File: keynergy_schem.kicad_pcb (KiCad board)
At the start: 2 copper layers, 0 parts

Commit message: new updates
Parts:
- added REF**: Solenoid Key, project library:Untitled, F.Cu at (56.3, 88.2)

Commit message: new update
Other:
- board outline added: 196 x 79.8 mm
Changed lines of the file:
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@@
 		(at 56.272 88.225312)
 		(property "Reference" "REF**"
-			(at 0 -0.5 0)
+			(at 0 8.128 0)
 			(unlocked yes)
 			(layer "F.SilkS")
@@
 		)
 		(property "Value" "Solenoid Key"
-			(at 0 1 0)
+			(at -0.127 9.652 0)
 			(unlocked yes)
 			(layer "F.Fab")
@@
 			(layer "F.SilkS")
 		)
+		(fp_rect
+			(start -4.4915 -4.4915)
+			(end 4.5085 4.5085)
+			(stroke
+				(width 0.05)
+				(type solid)
+			)
+			(fill yes)
+			(layer "Edge.Cuts")
+		)
 		(fp_text user "${REFERENCE}"
-			(at 0 2.5 0)
+			(at -0.254 11.43 0)
 			(unlocked yes)
 			(layer "F.Fab")
@@
 		)
 		(pad "1" smd roundrect
-			(at -14.4145 -0.0635)
-			(size 2.159 7.493)
+			(at -14.4145 0)
+			(size 2.159 7.366)
 			(layers "F.Cu" "F.Mask" "F.Paste")
 			(roundrect_rratio 0)
@@
 	)
 	(gr_rect
-		(start 26.1 23.6)
-		(end 222.1 98.3)
-		(stroke
-			(width 0.2)
-			(type default)
-		)
-		(fill no)
-		(layer "F.Cu")
-	)
-	(gr_rect
 		(start 123.6 56)
 		(end 125.1 61.8)
@@
 	)
 	(gr_rect
+		(start 26.1 23.6)
+		(end 222.1 103.38)
+		(stroke
+			(width 0.2)
+			(type solid)
+		)
+		(fill no)
+		(layer "Edge.Cuts")
+	)
+	(gr_rect

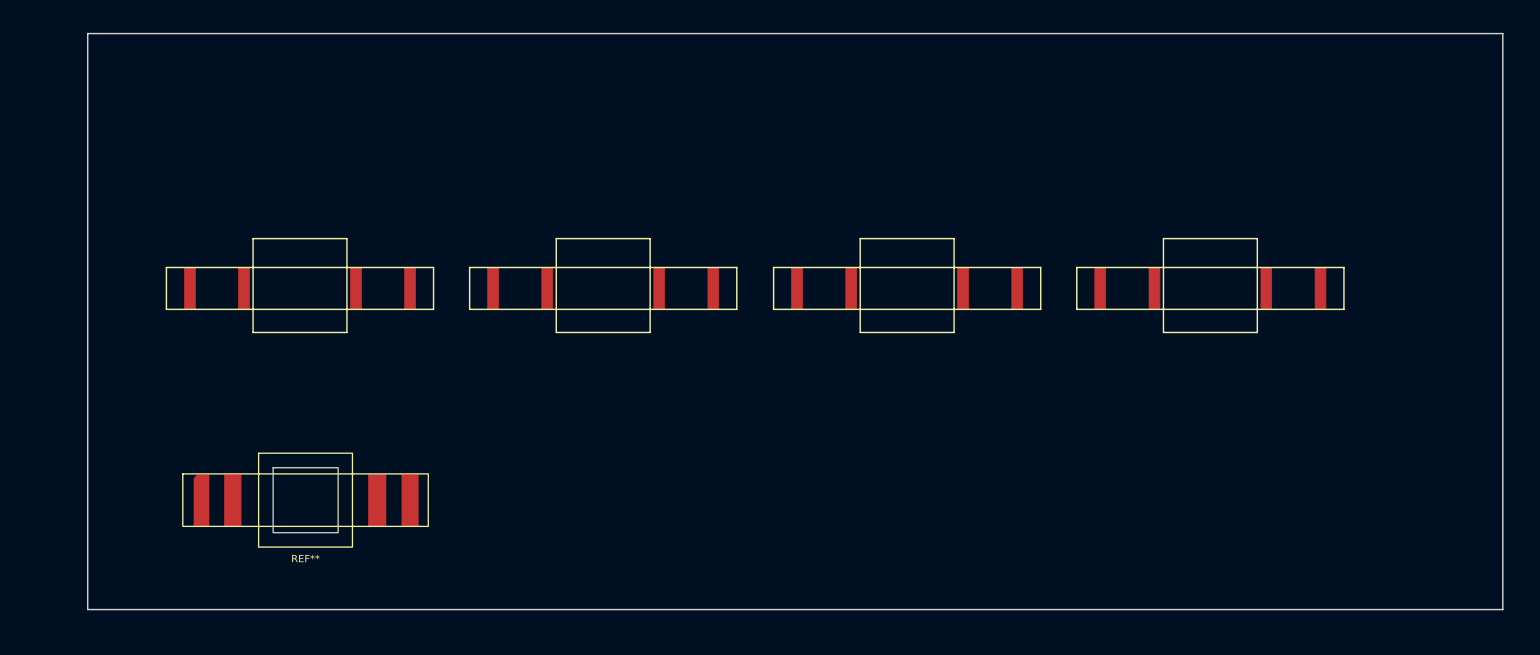
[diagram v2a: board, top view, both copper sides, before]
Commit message: custom selonoid key added
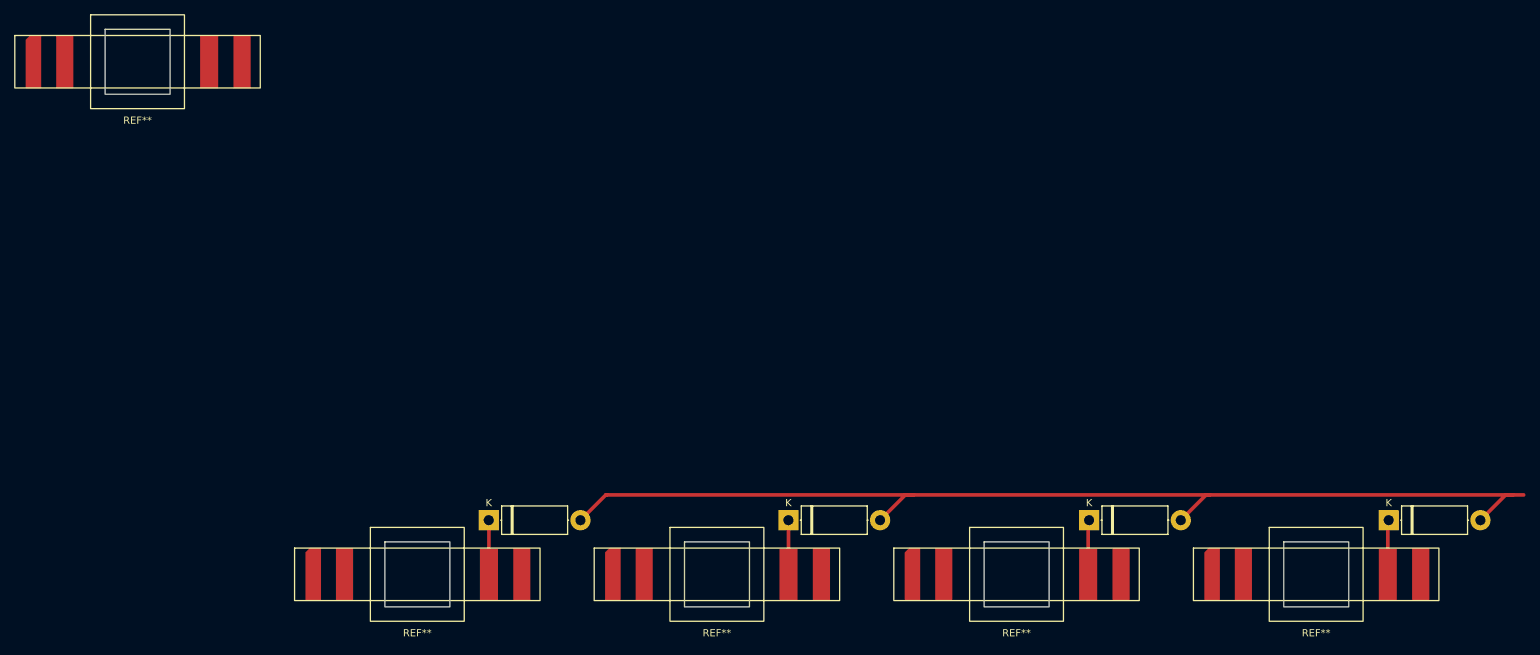
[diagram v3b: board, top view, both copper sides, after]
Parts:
- added Diode: Diode, Diode_THT:D_5W_P12.70mm_Horizontal, F.Cu at (164.8, 91.0)
- added Diode: Diode, Diode_THT:D_5W_P12.70mm_Horizontal, F.Cu at (81.7, 91.0)
- added Diode: Diode, Diode_THT:D_5W_P12.70mm_Horizontal, F.Cu at (206.3, 91.0)
- added Diode: Diode, Diode_THT:D_5W_P12.70mm_Horizontal, F.Cu at (123.2, 91.0)
- added REF**: Solenoid Key, project library:Untitled, F.Cu at (196.2, 98.5)
- added REF**: Solenoid Key, project library:Untitled, F.Cu at (154.8, 98.5)
- added REF**: Solenoid Key, project library:Untitled, F.Cu at (71.8, 98.5)
- added REF**: Solenoid Key, project library:Untitled, F.Cu at (113.2, 98.5)
- moved REF** 65.0 mm to (33.0, 27.5)
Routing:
- net (no net): track 0.00 -> 180.9 mm
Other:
- board size 196 x 79.8 mm -> 9 x 9 mm

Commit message: new files
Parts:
- removed Diode (x4): Diode, Diode_THT:D_5W_P12.70mm_Horizontal
- removed the REF** at (196.2, 98.5)
- removed the REF** at (154.8, 98.5)
- removed the REF** at (71.8, 98.5)
- removed the REF** at (113.2, 98.5)
- added D1: D, Diode_THT:D_DO-35_SOD27_P7.62mm_Horizontal, F.Cu at (73.0, 112.2)
- added D2: D, Diode_THT:D_DO-35_SOD27_P7.62mm_Horizontal, F.Cu at (128.0, 112.3)
- added D3: D, Diode_THT:D_DO-35_SOD27_P7.62mm_Horizontal, F.Cu at (184.0, 112.1)
- added D4: D, Diode_THT:D_DO-35_SOD27_P7.62mm_Horizontal, F.Cu at (239.5, 111.6)
- added J1: Conn_01x03_Pin, Connector_PinHeader_2.54mm:PinHeader_1x03_P2.54mm_Vertical, F.Cu at (264.5, 67.0)
- added J3: Columns, Connector_PinHeader_2.54mm:PinHeader_1x04_P2.54mm_Vertical, F.Cu at (26.0, 115.5)
- added J3: Conn_01x04_Pin, Connector_PinHeader_2.54mm:PinHeader_1x04_P2.54mm_Vertical, F.Cu at (32.0, 115.5)
- added Jumper: SolderWire-0.1sqmm_1x01_D0.4mm_OD1mm_Relief, Connector_Wire:SolderWire-0.1sqmm_1x01_D0.4mm_OD1mm_Relief, F.Cu at (115.0, 113.5)
- added Jumper: SolderWire-0.1sqmm_1x01_D0.4mm_OD1mm_Relief, Connector_Wire:SolderWire-0.1sqmm_1x01_D0.4mm_OD1mm_Relief, F.Cu at (171.0, 114.0)
- added Jumper: SolderWire-0.1sqmm_1x01_D0.4mm_OD1mm_Relief, Connector_Wire:SolderWire-0.1sqmm_1x01_D0.4mm_OD1mm_Relief, F.Cu at (226.5, 113.5)
- added K1: ~, project library:Solenoid Key, F.Cu at (59.5, 95.0)
- added K2: ~, project library:Solenoid Key, F.Cu at (115.0, 95.0)
- added K3: ~, project library:Solenoid Key, F.Cu at (171.1, 94.6)
- added K4: ~, project library:Solenoid Key, F.Cu at (226.5, 94.1)
- moved REF** 98.7 mm to (112.5, -31.0)
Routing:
- net Row 1: track 0.00 -> 255.8 mm
- net Row 3: track 0.00 -> 207.6 mm
- net Col 4: track 0.00 -> 207.0 mm
- net (no net): track 180.9 -> 0.00 mm
- net Col 3: track 0.00 -> 151.0 mm
- net Col 2: track 0.00 -> 94.1 mm, vias 0 -> 1
- net Net-(K2-C2): track 0.00 -> 58.1 mm
- net Net-(K3-C2): track 0.00 -> 57.7 mm
- net Net-(K1-C2): track 0.00 -> 57.4 mm
- net Row 2: track 0.00 -> 46.3 mm
- net Col 1: track 0.00 -> 37.5 mm
- net Net-(D1-A): track 0.00 -> 13.7 mm
- net Net-(D2-A): track 0.00 -> 13.2 mm
- net Net-(D4-A): track 0.00 -> 13.0 mm
- net Net-(D3-A): track 0.00 -> 13.0 mm

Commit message: new files
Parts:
- added D10: D, Diode_THT:D_DO-35_SOD27_P7.62mm_Horizontal, F.Cu at (363.5, 200.8)
- added D11: D, Diode_THT:D_DO-35_SOD27_P7.62mm_Horizontal, F.Cu at (362.5, 132.3)
- added D5: D, Diode_THT:D_DO-35_SOD27_P7.62mm_Horizontal, F.Cu at (71.5, 160.3)
- added D6: D, Diode_THT:D_DO-35_SOD27_P7.62mm_Horizontal, F.Cu at (128.5, 159.3)
- added D7: D, Diode_THT:D_DO-35_SOD27_P7.62mm_Horizontal, F.Cu at (184.0, 158.8)
- added D8: D, Diode_THT:D_DO-35_SOD27_P7.62mm_Horizontal, F.Cu at (99.0, 243.8)
- added D9: D, Diode_THT:D_DO-35_SOD27_P7.62mm_Horizontal, F.Cu at (183.5, 243.7)
- added J2: Coils, Connector_PinHeader_2.54mm:PinHeader_1x03_P2.54mm_Vertical, F.Cu at (202.0, 109.5)
- added J3: Columns, Connector_PinHeader_2.54mm:PinHeader_1x04_P2.54mm_Vertical, F.Cu at (25.5, 162.0)
- added J3: Columns, Connector_PinHeader_2.54mm:PinHeader_1x04_P2.54mm_Vertical, F.Cu at (331.5, 218.0)
- added J3: Columns, Connector_PinHeader_2.54mm:PinHeader_1x04_P2.54mm_Vertical, F.Cu at (25.5, 246.0)
- added J4: Conn_01x04_Pin, Connector_PinHeader_2.54mm:PinHeader_1x04_P2.54mm_Vertical, F.Cu at (30.5, 162.0)
- added J5: Conn_01x04_Pin, Connector_PinHeader_2.54mm:PinHeader_1x04_P2.54mm_Vertical, F.Cu at (31.0, 246.2)
- added J6: Conn_01x03_Pin, Connector_PinHeader_2.54mm:PinHeader_1x03_P2.54mm_Vertical, F.Cu at (201.6, 192.5)
- added J7: Conn_01x04_Pin, Connector_PinHeader_2.54mm:PinHeader_1x04_P2.54mm_Vertical, F.Cu at (331.5, 214.5)
- added J8: Conn_01x03_Pin, Connector_PinHeader_2.54mm:PinHeader_1x03_P2.54mm_Vertical, F.Cu at (373.1, 79.0)
- added Jumper: SolderWire-0.1sqmm_1x01_D0.4mm_OD1mm_Relief, Connector_Wire:SolderWire-0.1sqmm_1x01_D0.4mm_OD1mm_Relief, F.Cu at (342.5, 126.5)
- added Jumper: SolderWire-0.1sqmm_1x01_D0.4mm_OD1mm_Relief, Connector_Wire:SolderWire-0.1sqmm_1x01_D0.4mm_OD1mm_Relief, F.Cu at (345.5, 126.5)
- added Jumper: SolderWire-0.1sqmm_1x01_D0.4mm_OD1mm_Relief, Connector_Wire:SolderWire-0.1sqmm_1x01_D0.4mm_OD1mm_Relief, F.Cu at (171.5, 160.0)
- added Jumper: SolderWire-0.1sqmm_1x01_D0.4mm_OD1mm_Relief, Connector_Wire:SolderWire-0.1sqmm_1x01_D0.4mm_OD1mm_Relief, F.Cu at (115.4, 160.5)
- added Jumper: SolderWire-0.1sqmm_1x01_D0.4mm_OD1mm_Relief, Connector_Wire:SolderWire-0.1sqmm_1x01_D0.4mm_OD1mm_Relief, F.Cu at (171.0, 244.4)
- added Jumper: SolderWire-0.1sqmm_1x01_D0.4mm_OD1mm_Relief, Connector_Wire:SolderWire-0.1sqmm_1x01_D0.4mm_OD1mm_Relief, F.Cu at (334.0, 195.5)
- added Jumper: SolderWire-0.1sqmm_1x01_D0.4mm_OD1mm_Relief, Connector_Wire:SolderWire-0.1sqmm_1x01_D0.4mm_OD1mm_Relief, F.Cu at (342.5, 138.5)
- added K10: ~, project library:Solenoid Key, F.Cu at (353.0, 183.5)
- added K11: ~, project library:Solenoid Key, F.Cu at (353.5, 115.0)
- added K5: ~, project library:Solenoid Key, F.Cu at (59.0, 142.6)
- added K6: ~, project library:Solenoid Key, F.Cu at (115.4, 141.9)
- added K7: ~, project library:Solenoid Key, F.Cu at (171.4, 141.4)
- added K8: ~, project library:Solenoid Key, F.Cu at (86.0, 226.0)
- added K9: ~, project library:Solenoid Key, F.Cu at (171.0, 226.0)
- moved D1 37.5 mm to (72.5, 74.7)
- moved D2 37.5 mm to (127.5, 74.9)
- moved D3 37.5 mm to (183.5, 74.7)
- moved D4 37.5 mm to (239.0, 74.2)
- moved J3 37.5 mm to (25.5, 78.0)
- moved J3 37.5 mm to (31.5, 78.0)
- moved Jumper 37.5 mm to (114.5, 76.0)
- moved Jumper 37.5 mm to (170.5, 76.6)
- moved Jumper 37.5 mm to (226.0, 76.1)
- moved K1 37.5 mm to (59.0, 57.5)
- moved K2 37.5 mm to (114.5, 57.5)
- moved K3 37.5 mm to (170.6, 57.1)
- moved J1 37.5 mm to (264.0, 29.5)
- moved K4 37.5 mm to (226.0, 56.6)
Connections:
- net Col 1 renamed Col 1-1
- net Col 2 renamed Col 1-2
- net Col 3 renamed Col 1-3
- net Col 4 renamed Col 1-4
- net Row 2 renamed Coil 1-1
- net Row 3 renamed Coil 1-2
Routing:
- net Row 2: track 0.00 -> 189.1 mm
- net Row 5: track 0.00 -> 161.7 mm
- net Coil 2-2: track 0.00 -> 152.4 mm
- net Col 2-3: track 0.00 -> 151.7 mm
- net Col 5-2: track 0.00 -> 150.3 mm
- net Col 5: track 0.00 -> 140.6 mm
- net Coil 5-2: track 0.00 -> 124.2 mm
- net Coil 5-4: track 0.00 -> 109.4 mm
- net Row 5-2: track 0.00 -> 100.6 mm
- net Col 2-2: track 0.00 -> 94.9 mm
- net Net-(K8-C2): track 0.00 -> 87.0 mm
- net Net-(K10-C2): track 0.00 -> 79.0 mm
- net Col 5-1: track 0.00 -> 65.3 mm
- net Net-(K5-C2): track 0.00 -> 58.6 mm
- net Net-(K6-C2): track 0.00 -> 58.1 mm
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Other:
- board text added: "Addition"
- board text added: "Col 1"
- board text added: "Col 1-2"
- board text added: "Col 2"
- board text added: "Col 3"
- board text added: "Col 4"
- board text added: "Col 4-1"
- board text added: "Col 4-2"
- board text added: "Division"
- board text added: "Eight Five Two"
- board text added: "Enter"
- board text added: "Multiplication"
- board text added: "Nine Six Three"
- board text added: "Num Lock"
- board text added: "Period"
- board text added: "Row 1"
- board text added: "Row 2-4"
- board text added: "Row 5"
- board text added: "Seven Four One"
- board text added: "Subtraction"
- board text added: "Zero"

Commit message: new
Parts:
- removed REF**: Solenoid Key, project library:Untitled
- moved K4 303.4 mm to (525.5, 8.08)
- moved K1 303.4 mm to (358.5, 8.96)
- moved D1 303.4 mm to (372.0, 26.2)
- moved D2 303.4 mm to (427.0, 26.3)
- moved D3 303.4 mm to (483.0, 26.1)
- moved D4 303.4 mm to (538.5, 25.6)
- moved J1 303.4 mm to (563.5, -19.0)
- moved J3 303.4 mm to (325.0, 29.5)
- moved J3 303.4 mm to (331.0, 29.5)
- moved Jumper 303.4 mm to (414.0, 27.5)
- moved Jumper 303.4 mm to (470.0, 28.0)
- moved Jumper 303.4 mm to (525.5, 27.5)
- moved K2 303.4 mm to (414.0, 9.00)
- moved K3 303.4 mm to (470.1, 8.58)
- moved J5 193.5 mm to (220.0, 287.7)
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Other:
- board outline removed
